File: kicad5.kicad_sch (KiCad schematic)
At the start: 7 parts, among them SW1 SW_Push, SW2 SW_Push, SW3 SW_Push, SW4 SW_Push, U1 XIAO-RP2040-DIP

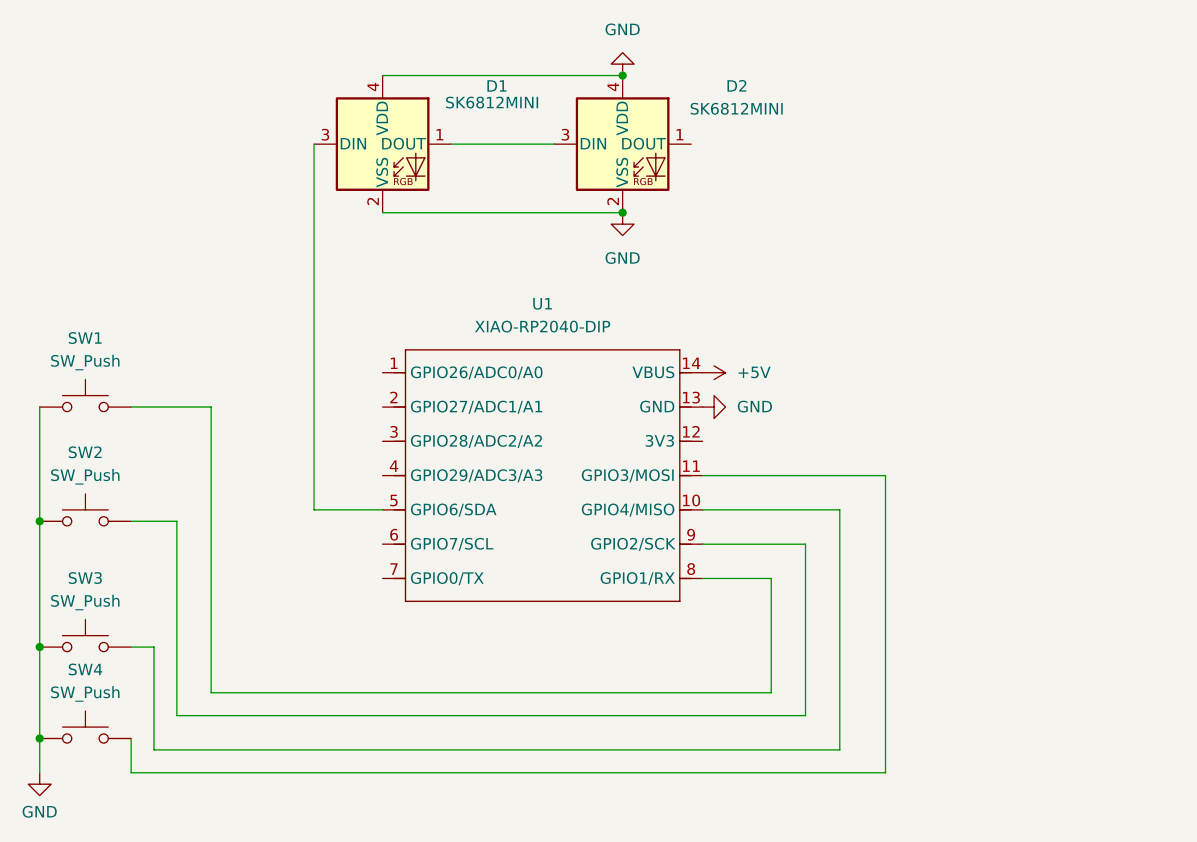
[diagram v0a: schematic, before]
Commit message: added ec11
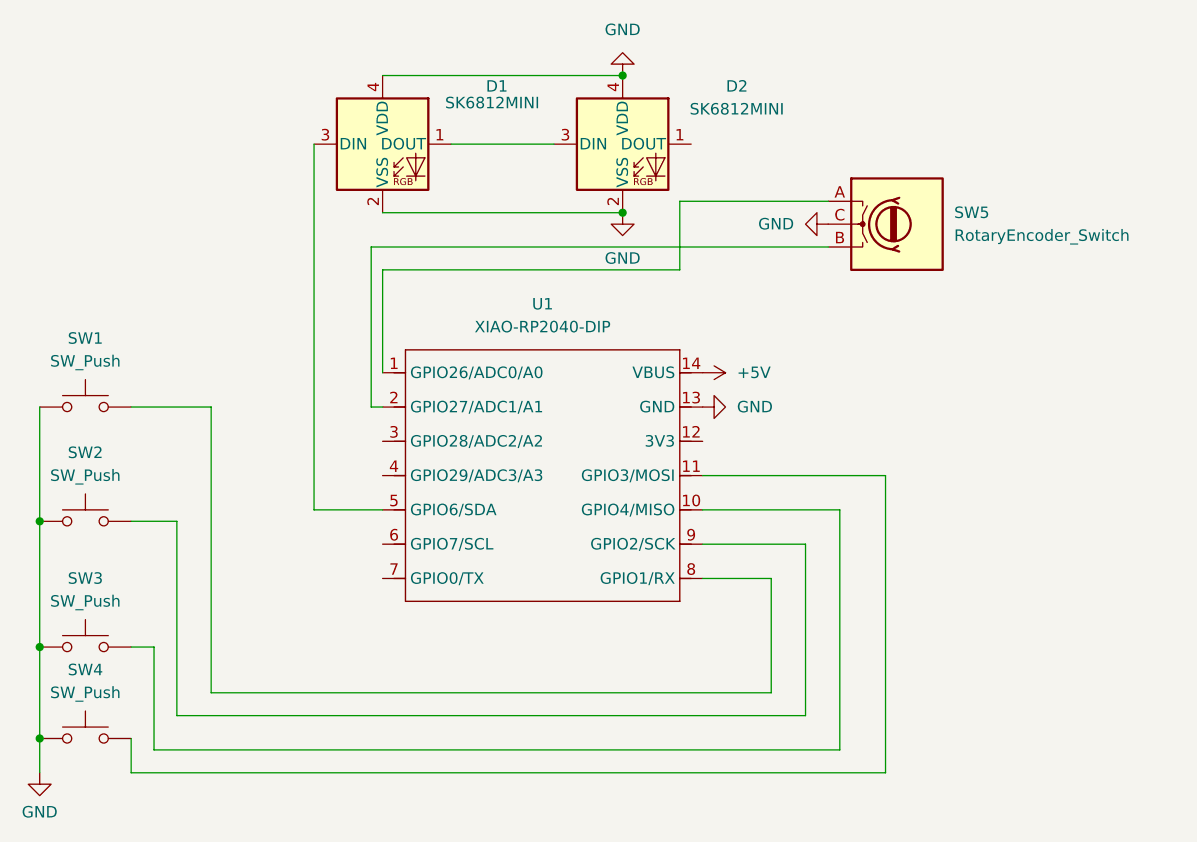
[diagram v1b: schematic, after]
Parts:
- added SW5: RotaryEncoder_Switch, ec11:RotaryEncoder_Alps_EC11E_Vertical_H20mm, symbol Device:RotaryEncoder
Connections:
- net GND: now also SW5.C
- net at U1.1 (GPIO26/ADC0/A0): now also SW5.A
- net at U1.2 (GPIO27/ADC1/A1): now also SW5.B
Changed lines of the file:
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@@
+	(wire
+		(pts
+			(xy 147.32 104.14) (xy 147.32 115.57)
+		)
+		(stroke
+			(width 0)
+			(type default)
+		)
+	)
 	(wire
 		(pts
@@
 	(wire
 		(pts
+			(xy 146.05 119.38) (xy 147.32 119.38)
+		)
+		(stroke
+			(width 0)
+			(type default)
+		)
+	)
+	(wire
+		(pts
 			(xy 190.5 151.13) (xy 128.27 151.13)
 		)
@@
 	(wire
 		(pts
+			(xy 196.85 96.52) (xy 180.34 96.52)
+		)
+		(stroke
+			(width 0)
+			(type default)
+		)
+	)
+	(wire
+		(pts
 			(xy 109.22 156.21) (xy 109.22 160.02)
 		)
@@
 	(wire
 		(pts
+			(xy 146.05 101.6) (xy 146.05 119.38)
+		)
+		(stroke
+			(width 0)
+			(type default)
+		)
+	)
+	(wire
+		(pts
 			(xy 198.12 130.81) (xy 198.12 157.48)
 		)
@@
 	(wire
 		(pts
+			(xy 180.34 96.52) (xy 180.34 104.14)
+		)
+		(stroke
+			(width 0)
+			(type default)
+		)
+	)
+	(wire
+		(pts
 			(xy 121.92 157.48) (xy 121.92 146.05)
 		)
@@
 	(wire
 		(pts
+			(xy 180.34 104.14) (xy 147.32 104.14)
+		)
+		(stroke
+			(width 0)
+			(type default)
+		)
+	)
+	(wire
+		(pts
 			(xy 139.7 90.17) (xy 139.7 130.81)
+		)
+		(stroke
+			(width 0)
+			(type default)
+		)
+	)
+	(wire
+		(pts
+			(xy 196.85 101.6) (xy 146.05 101.6)
 		)
 		(stroke
@@
 	)
 	(symbol
+		(lib_id "Device:RotaryEncoder")
+		(at 204.47 99.06 0)
+		(unit 1)
+		(exclude_from_sim no)
+		(in_bom yes)
+		(on_board yes)
+		(dnp no)
+		(fields_autoplaced yes)
+		(property "Reference" "SW5"
+			(at 210.82 97.7899 0)
+			(effects
+				(font
+					(size 1.27 1.27)
+				)
+				(justify left)
+			)
+		)
+		(property "Value" "RotaryEncoder_Switch"
+			(at 210.82 100.3299 0)
+			(effects
+				(font
+					(size 1.27 1.27)
+				)
+				(justify left)
+			)
+		)
+		(property "Footprint" "ec11:RotaryEncoder_Alps_EC11E_Vertical_H20mm"
+			(at 200.66 94.996 0)
+			(effects
+				(font
+					(size 1.27 1.27)
+				)
+				(hide yes)
+			)
+		)
+		(property "Datasheet" "~"
+			(at 204.47 92.456 0)
+			(effects
+				(font
+					(size 1.27 1.27)
+				)
+				(hide yes)
+			)
+		)
+		(property "Description" "Rotary encoder, dual channel, incremental quadrate outputs"
+			(at 204.47 99.06 0)
+			(effects
+				(font
+					(size 1.27 1.27)
+				)
+				(hide yes)
+			)
+		)
+		(pin "A"
+		)
+		(pin "B"
+		)
+		(pin "C"
+		)
+		(instances
+			(project ""
+				(path "/472758f6-d5d5-4d0b-9d72-f8340e59b8c2"
+					(reference "SW5")
+					(unit 1)
+				)
+			)
+		)
+	)
+	(symbol
 		(lib_id "power:+5V")
 		(at 182.88 115.57 270)
@@
 					(unit 1)
 				)
+			)
+		)
+	)
+	(symbol
+		(lib_id "power:GND")
+		(at 196.85 99.06 270)
+		(unit 1)
+		(exclude_from_sim no)
+		(in_bom yes)
+		(on_board yes)
+		(dnp no)
+		(fields_autoplaced yes)
+		(property "Reference" "#PWR06"
+			(at 190.5 99.06 0)
+			(effects
+				(font
+					(size 1.27 1.27)
+				)
+				(hide yes)
+			)
+		)
+		(property "Value" "GND"
+			(at 193.04 99.0599 90)
+			(effects
+				(font
+					(size 1.27 1.27)
+				)
+				(justify right)
+			)
+		)
+		(property "Footprint" ""
+			(at 196.85 99.06 0)
+			(effects
+				(font
+					(size 1.27 1.27)
+				)
+				(hide yes)
+			)
+		)
+		(property "Datasheet" ""
+			(at 196.85 99.06 0)
+			(effects
+				(font
+					(size 1.27 1.27)
+				)
+				(hide yes)
+			)
+		)
+		(property "Description" "Power symbol creates a global label with name \"GND\" , ground"
+			(at 196.85 99.06 0)
+			(effects
+				(font
+					(size 1.27 1.27)
+				)
+				(hide yes)
+			)
+		)
+		(pin "1"
+		)
+		(instances
+			(project ""
+				(path "/472758f6-d5d5-4d0b-9d72-f8340e59b8c2"
+					(reference "#PWR06")
+					(unit 1)
+				)
